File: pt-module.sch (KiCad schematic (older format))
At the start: 6 parts

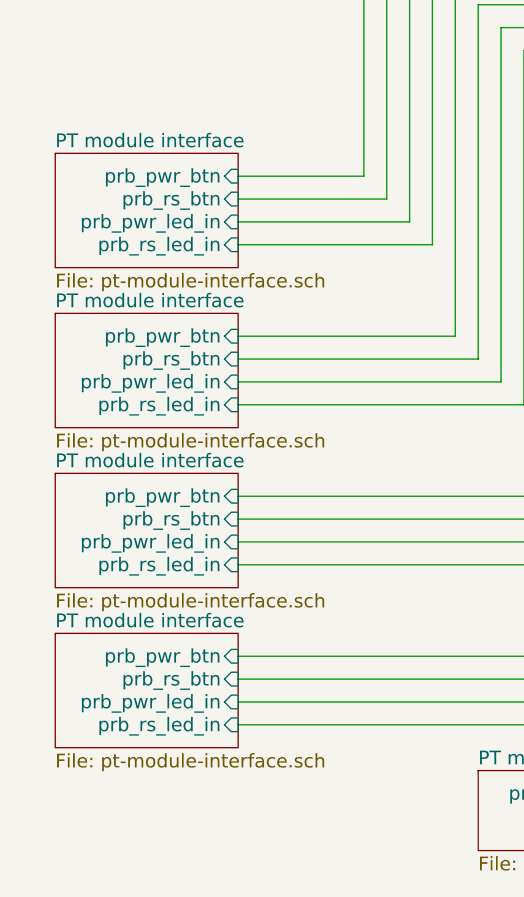
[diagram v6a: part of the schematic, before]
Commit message: indeces to interfacemodules
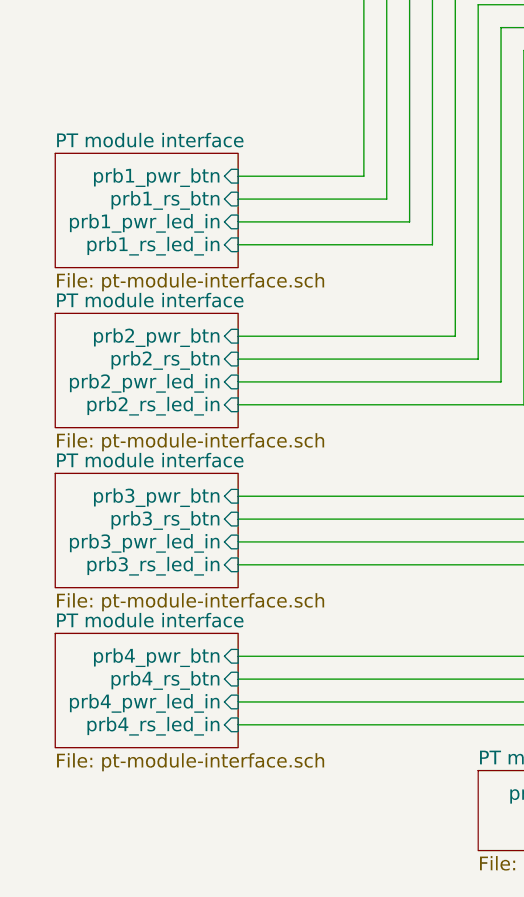
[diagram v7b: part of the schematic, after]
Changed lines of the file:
@@
 F0 "PT module interface" 60
 F1 "pt-module-interface.sch" 60
-F2 "prb_pwr_btn" I R 1400 4500 60
-F3 "prb_pwr_led_in" I R 1400 4700 60
-F4 "prb_rs_btn" I R 1400 4600 60
-F5 "prb_rs_led_in" I R 1400 4800 60
+F2 "prb1_pwr_btn" I R 1400 4500 60
+F3 "prb1_pwr_led_in" I R 1400 4700 60
+F4 "prb1_rs_btn" I R 1400 4600 60
+F5 "prb1_rs_led_in" I R 1400 4800 60
 $EndSheet
 $Comp
@@
 F0 "PT module interface" 60
 F1 "pt-module-interface.sch" 60
-F2 "prb_pwr_btn" I R 1400 5200 60
-F3 "prb_pwr_led_in" I R 1400 5400 60
-F4 "prb_rs_btn" I R 1400 5300 60
-F5 "prb_rs_led_in" I R 1400 5500 60
+F2 "prb2_pwr_btn" I R 1400 5200 60
+F3 "prb2_pwr_led_in" I R 1400 5400 60
+F4 "prb2_rs_btn" I R 1400 5300 60
+F5 "prb2_rs_led_in" I R 1400 5500 60
 $EndSheet
 $Sheet
@@
 F0 "PT module interface" 60
 F1 "pt-module-interface.sch" 60
-F2 "prb_pwr_btn" I R 1400 5900 60
-F3 "prb_pwr_led_in" I R 1400 6100 60
-F4 "prb_rs_btn" I R 1400 6000 60
-F5 "prb_rs_led_in" I R 1400 6200 60
+F2 "prb3_pwr_btn" I R 1400 5900 60
+F3 "prb3_pwr_led_in" I R 1400 6100 60
+F4 "prb3_rs_btn" I R 1400 6000 60
+F5 "prb3_rs_led_in" I R 1400 6200 60
 $EndSheet
 $Sheet
@@
 F0 "PT module interface" 60
 F1 "pt-module-interface.sch" 60
-F2 "prb_pwr_btn" I R 1400 6600 60
-F3 "prb_pwr_led_in" I R 1400 6800 60
-F4 "prb_rs_btn" I R 1400 6700 60
-F5 "prb_rs_led_in" I R 1400 6900 60
-$EndSheet
-Wire Wire Line
+F2 "prb4_pwr_btn" I R 1400 6600 60
+F3 "prb4_pwr_led_in" I R 1400 6800 60
+F4 "prb4_rs_btn" I R 1400 6700 60
+F5 "prb4_rs_led_in" I R 1400 6900 60
+$EndSheet
+Wire Wire Line

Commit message: I don't know what I did
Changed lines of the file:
@@
 $EndSheet
 $Sheet
-S 7100 4650 1000 1050
+S 5850 3750 1000 700
 U 598183C5
 F0 "Probe module" 60
 F1 "probe_module.sch" 60
-F2 "prb1_pwr_ctrl" I R 8100 4750 60
-F3 "prb1_rs_ctrl" I R 8100 4850 60
-F4 "prb2_rs_ctrl" I R 8100 5150 60
-F5 "prb2_pwr_ctrl" I R 8100 5450 60
-F6 "vaisala_rs485_a" I R 8100 4950 60
-F7 "vaisala_rs485_b" I R 8100 5050 60
+F2 "prb1_pwr_ctrl" I L 5850 3850 60
+F3 "prb1_rs_ctrl" I L 5850 3950 60
+F4 "prb2_rs_ctrl" I L 5850 4050 60
+F5 "prb2_pwr_ctrl" I L 5850 4150 60
+F6 "vaisala_rs485_a" I R 6850 4350 60
+F7 "vaisala_rs485_b" I R 6850 4250 60
 $EndSheet
 $Sheet
